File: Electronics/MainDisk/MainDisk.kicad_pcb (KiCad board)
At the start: 2 copper layers, 38 x 38 mm, 36 parts, among them J1 Conn_02x03_Odd_Even, Q1 Q_NPN_BEC, SW1 SW_Push, SW2 SW_SPST, U1 ATMEGA328PB-AURCT-ND, U2 TSOP4840-ND, Y1 535-10212-1-ND

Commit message: Continued work on the Disk
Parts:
- removed C5, C6: 1uF, Capacitor_SMD:C_0805_2012Metric
- added D5: LED, LED_SMD:LED_0805_2012Metric, F.Cu at (165.7, 66.9)
- added D6: LED, LED_SMD:LED_0805_2012Metric, F.Cu at (165.7, 68.8)
- added R4: 470R, Resistor_SMD:R_0805_2012Metric, F.Cu at (162.8, 66.9)
- added R5: 470R, Resistor_SMD:R_0805_2012Metric, F.Cu at (162.8, 68.8)
- added R6: 100k, Resistor_SMD:R_0805_2012Metric, F.Cu at (159.5, 74.6)
- added R7: 30k, Resistor_SMD:R_0805_2012Metric, F.Cu at (156.2, 74.6)
- added R8: 100k, Resistor_SMD:R_0805_2012Metric, F.Cu at (159.0, 65.4)
- added SW3: SW_Push, Button_Switch_SMD:SW_SPST_B3U-1000P, F.Cu at (165.8, 71.3)
- R3: value R_Small -> 470R
- moved C4 3.18 mm to (145.8, 73.4), turned to 270 degrees
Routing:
- net Net-(D6-Pad1): track 0.00 -> 20.9 mm, vias 0 -> 1
- net Net-(D5-Pad1): track 0.00 -> 19.1 mm, vias 0 -> 1
- net /RESET: track 16.3 -> 23.3 mm
- net /BAT_SENS: track 0.00 -> 6.22 mm, vias 0 -> 1
- net +BATT: track 147.4 -> 151.5 mm
- net Net-(D6-Pad2): track 0.00 -> 1.43 mm
- net Net-(D5-Pad2): track 0.00 -> 1.43 mm
- net /SCL: track 16.4 -> 17.7 mm
- net GND: vias 2 -> 4
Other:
- board size 38 x 38 mm -> 37.8 x 37.8 mm
- board text added: "+"
- board text added: "-"
- board text added: "1"
- board text added: "16"
- board text added: "2"
- board text added: "4"
- board text added: "8"
- board text added: "ADDR"
- board text added: "ERR"
- board text added: "PWR"
- board text added: "RST"
- board text added: "RX"
- board text added: "SCL"
- board text added: "SDA"
- board text added: "TX"

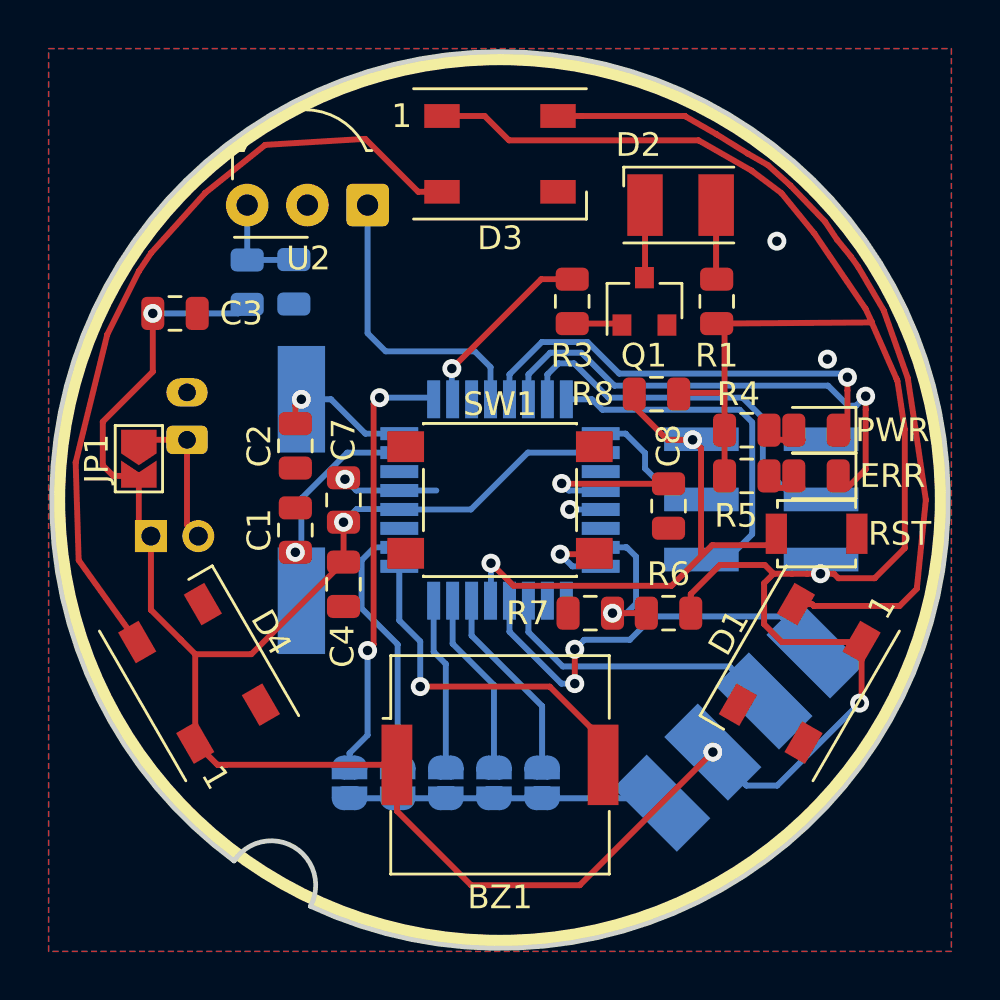
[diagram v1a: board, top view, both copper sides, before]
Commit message: More smol tweaks to the bacon
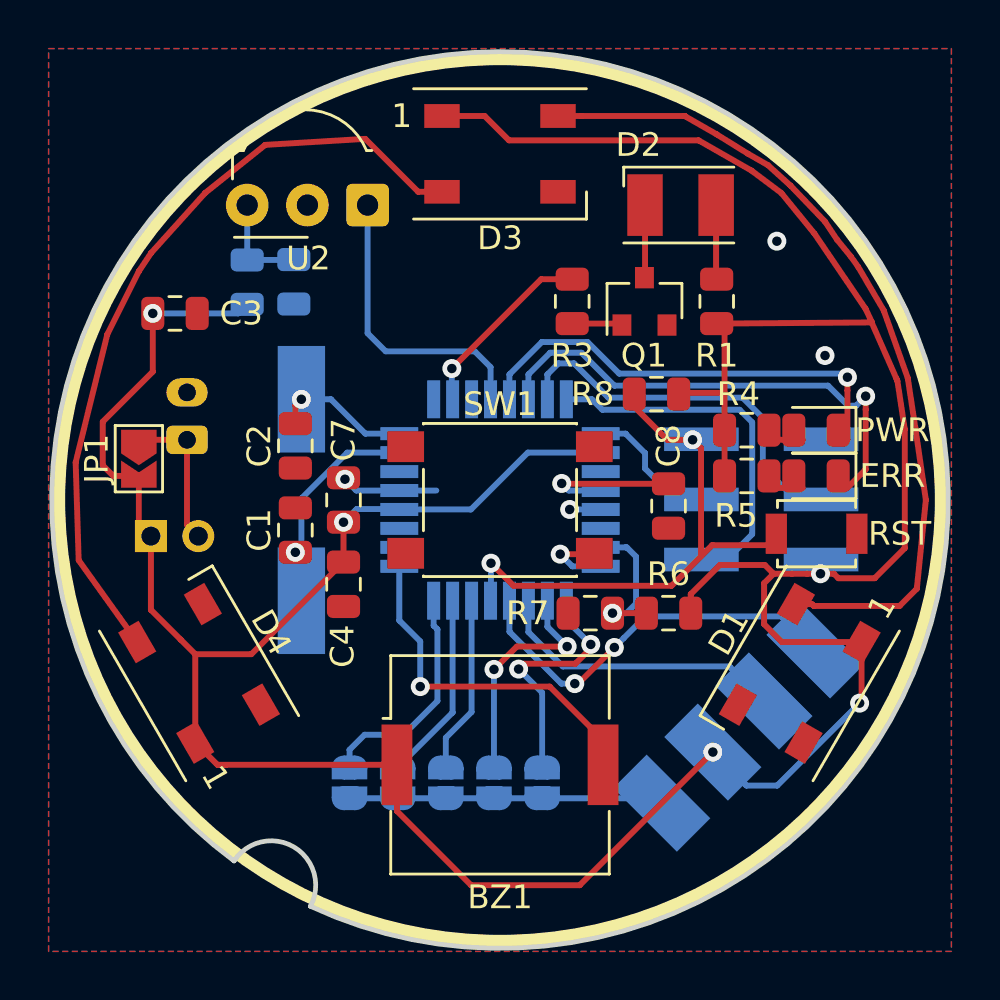
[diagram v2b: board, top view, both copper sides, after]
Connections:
- U1 pad 2: Net-(JP5-Pad1) -> Net-(U1-Pad2)
- U1 pad 25: Net-(U1-Pad25) -> Net-(JP2-Pad1)
- U1 pad 26: Net-(U1-Pad26) -> Net-(JP3-Pad1)
- U1 pad 30: Net-(JP2-Pad1) -> Net-(JP4-Pad1)
- U1 pad 31: Net-(JP3-Pad1) -> Net-(JP5-Pad1)
- U1 pad 32: Net-(JP4-Pad1) -> Net-(JP6-Pad1)
- U1 pad 9: Net-(JP6-Pad1) -> Net-(U1-Pad9)
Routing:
- net Net-(JP6-Pad1): track 18.4 -> 9.61 mm, vias 2 -> 0
- net Net-(JP5-Pad1): track 11.2 -> 8.00 mm
- net Net-(JP3-Pad1): track 7.76 -> 10.1 mm, vias 0 -> 2
- net Net-(JP2-Pad1): track 8.27 -> 10.4 mm, vias 0 -> 2
- net /SCL: track 17.7 -> 16.9 mm
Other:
- board text added: "A0"
- board text added: "A1"

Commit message: More or less Rev. 1
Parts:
- added J2: Conn_01x02_Male, Connector_PinHeader_2.00mm:PinHeader_1x02_P2.00mm_Vertical, B.Cu at (161.0, 57.4)
- J1: value Conn_02x03_Odd_Even -> 0015912060
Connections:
- D1 pad 4: Net-(D1-Pad4) -> /WS2812
- U1 pad 2: Net-(U1-Pad2) -> /WS2812
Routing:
- net /WS2812: track 0.00 -> 23.0 mm, vias 0 -> 1
- net +BATT: track 151.5 -> 149.5 mm
- net /BZR: track 15.1 -> 14.5 mm
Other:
- outline, holes or cut-outs redrawn
